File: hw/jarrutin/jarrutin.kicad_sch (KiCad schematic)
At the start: 24 parts, among them Q1 IR FET, Q2 IRFIZ34NPdF, U1 40106, U2 TC4422, U3 L7805, U4 Pico

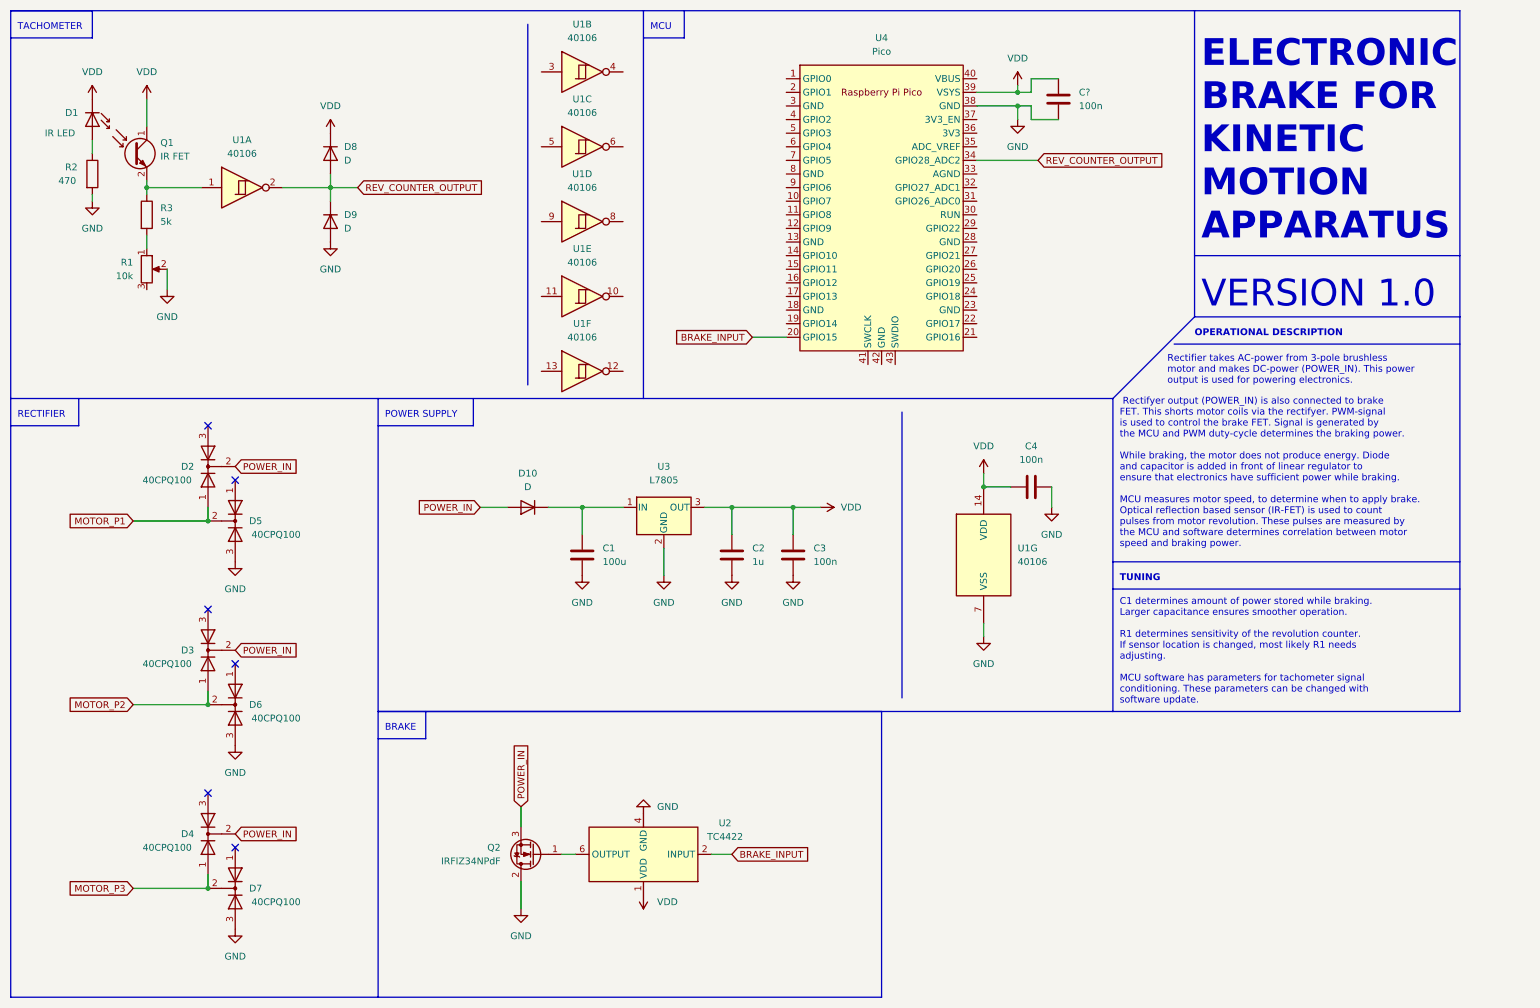
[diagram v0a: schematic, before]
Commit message: Adds BOM and updates HW design
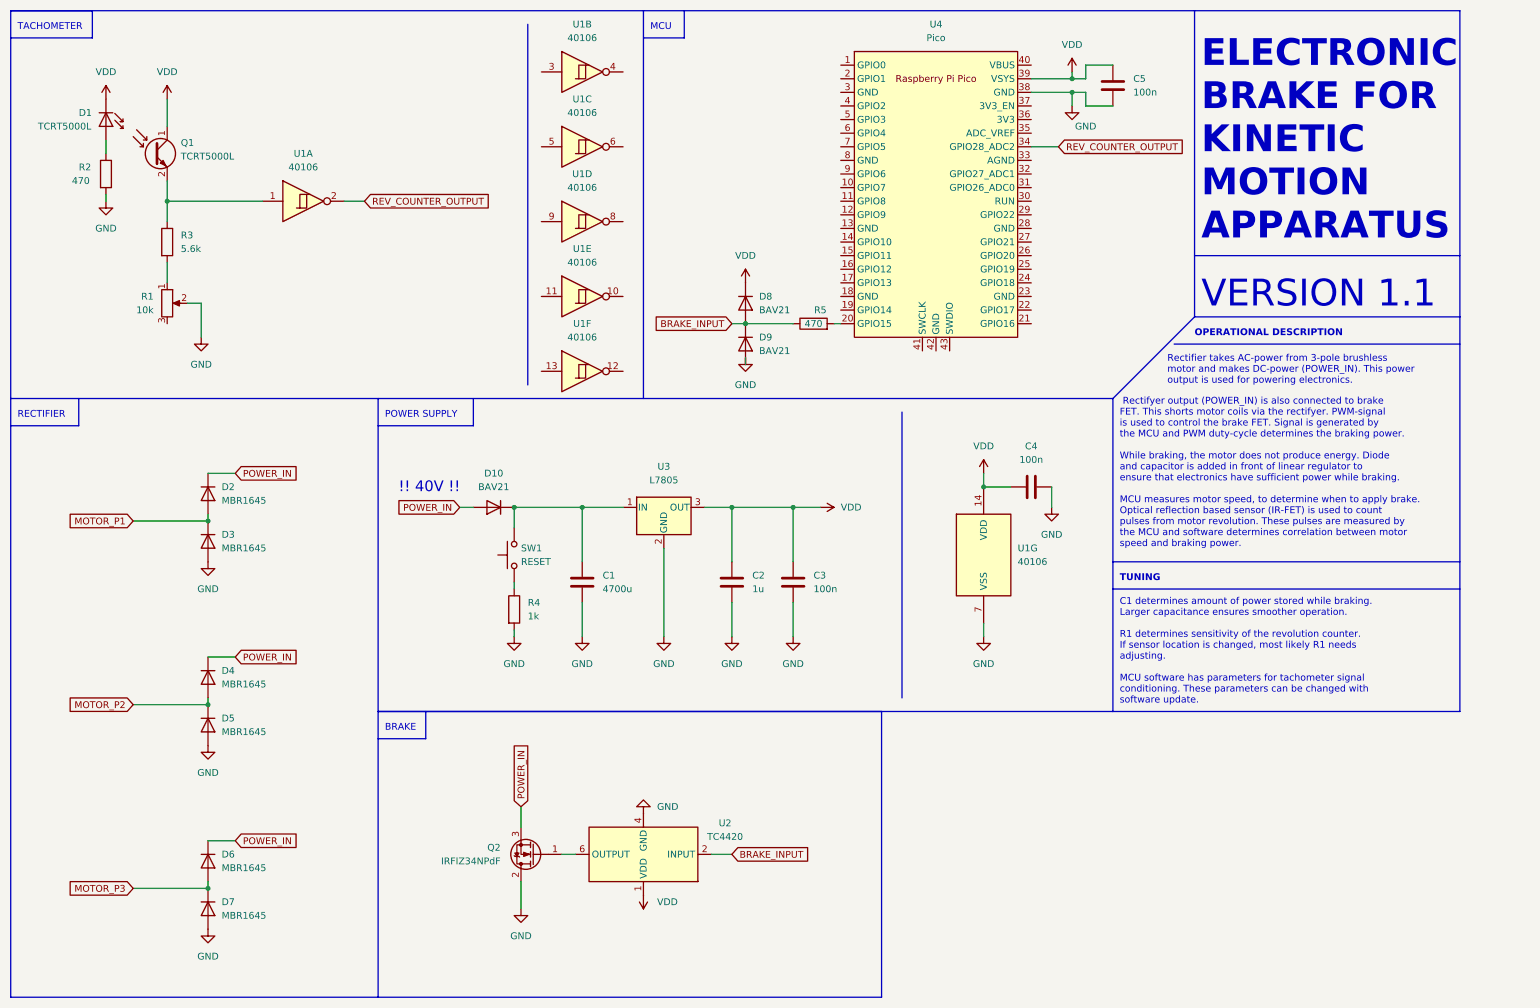
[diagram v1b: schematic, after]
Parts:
- removed D2, D3, D4, D5, D6, D7: 40CPQ100, Package_TO_SOT_THT:TO-247-3_Vertical, symbol Diode:BAV70W
- added D2, D3, D4, D5, D6, D7: MBR1645, symbol Device:D
- added R4: 1k, symbol Device:R
- added R5: 470, symbol Device:R
- added SW1: RESET, symbol Switch:SW_Push
- C1: value 100u -> 4700u
- D1: value IR LED -> TCRT5000L
- D10, D8, D9: value D -> BAV21
- Q1: value IR FET -> TCRT5000L
- R3: value 5k -> 5.6k
- U2: value TC4422 -> TC4420
- gave numbers to parts that had none: 1
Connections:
- net BRAKE_INPUT: now also D8.2 (A), D9.1 (K), R5.1; no longer U4.20 (GPIO15)
- net GND: now also D3.2 (A), D5.2 (A), D7.2 (A), R4.2
- net MOTOR_P1: now also D2.2 (A), D3.1 (K)
- net MOTOR_P2: now also D4.2 (A), D5.1 (K)
- net MOTOR_P3: now also D6.2 (A), D7.1 (K)
- net POWER_IN: now also D2.1 (K), D4.1 (K), D6.1 (K)
- net REV_COUNTER_OUTPUT: no longer D8.2 (A), D9.1 (K)
- net at C1.1, D10.1 (K), U3.1 (IN): now also SW1.2
- new net: R4.1, SW1.1
- new net: R5.2, U4.20 (GPIO15)
- no-connect marks 6 -> 0
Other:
- note added: "!! 40V !!"
- note added: "VERSION 1.1"
- note removed: "VERSION 1.0"
- moved on the sheet: C1, C2, C3, C5, D1, D10, Q1, R1, R2, R3, U1A, U4

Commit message: Updated schematic
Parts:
- added D11: INDICATOR, symbol LED:IR204A
- R4: value 1k -> 5.6k
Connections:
- net BRAKE_INPUT: now also U4.20 (GPIO15); no longer D8.2 (A), D9.1 (K), R5.1
- net GND: now also D11.1 (K)
- net REV_COUNTER_OUTPUT: now also D8.2 (A), D9.1 (K), R5.2; no longer U4.34 (GPIO28_ADC2)
- net at U4.4 (GPIO2): now also D11.2 (A)
- new net: R5.1, U4.34 (GPIO28_ADC2)
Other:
- note added: "C1 determines amount of power stored while braking. Larger capacitance ensures smoother operation. Too large capacitance will slow CPU boot-up time. R1 determines sensitivity of the revolution counter. If sensor location is changed, most likely R1 needs adjusting. 7.5kOhm (between pins 1 and 2) is good starting point. MCU software has parameters for tachometer signal conditioning. These parameter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"
- note added: "VERSION 1.2"
- note removed: "C1 determines amount of power stored while braking. Larger capacitance ensures smoother operation. R1 determines sensitivity of the revolution counter. If sensor location is changed, most likely R1 needs adjusting. MCU software has parameters for tachometer signal conditioning. These parameters can be changed with software update."
- note removed: "VERSION 1.1"
- moved on the sheet: C5, D8, D9, R5, U4

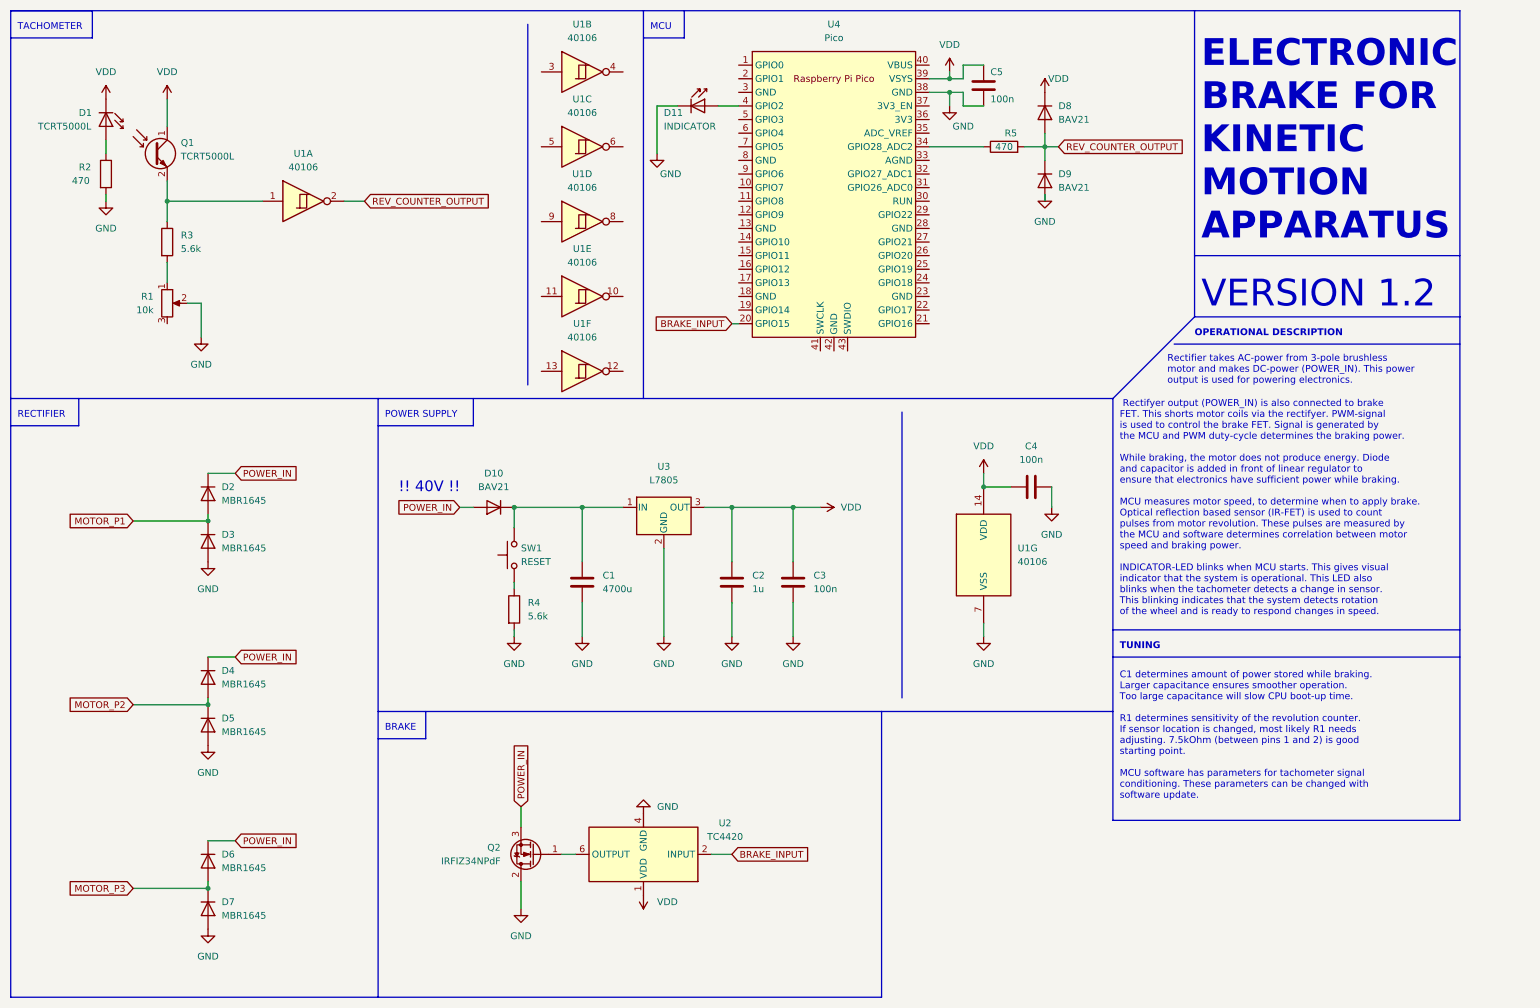
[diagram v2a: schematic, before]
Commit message: Update based on final implementation
Updated design, based on tests done 19.01.24. Functionality of hardware and software has been proven and the remaining issue is getting rid of dissipated power from diodes and FETs.
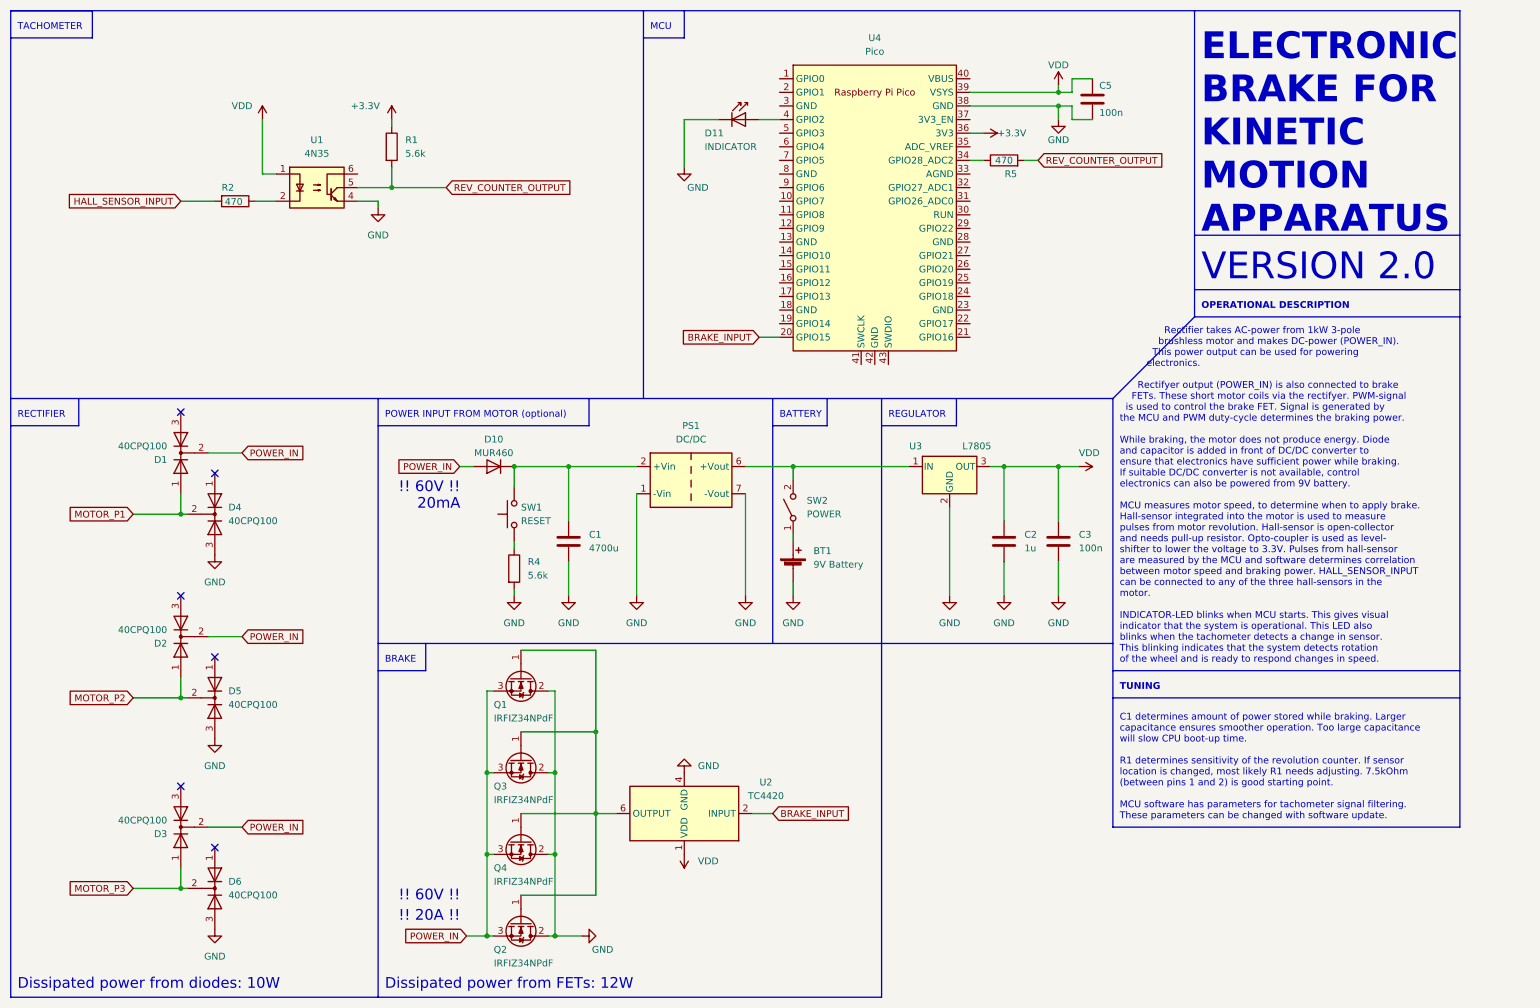
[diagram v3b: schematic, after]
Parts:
- removed C4: 100n, symbol Device:C
- removed D1: TCRT5000L, LED_THT:LED_D3.0mm_IRBlack, symbol LED:IR204A
- removed D2, D3, D4, D5, D6, D7: MBR1645, symbol Device:D
- removed D8, D9: BAV21, symbol Device:D
- removed Q1: TCRT5000L, LED_THT:LED_D5.0mm_Clear, symbol Sensor_Optical:BP103BF
- removed R1: 10k, symbol Device:R_Potentiometer
- removed R3: 5.6k, symbol Device:R
- removed U1: 40106, symbol 4xxx:40106
- added BT1: 9V Battery, symbol Device:Battery_Cell
- added D1, D2, D3, D4, D5, D6: 40CPQ100, symbol Device:D_Dual_CommonCathode_AAK
- added PS1: DC/DC, Converter_DCDC:Converter_DCDC_XP_POWER-ITXxxxxSA_THT, symbol Converter_DCDC:ITX0512SA
- added Q1, Q3, Q4: IRFIZ34NPdF, Package_TO_SOT_THT:TO-220-3_Vertical, symbol Transistor_FET:IRF540N
- added R1: 5.6k, symbol Device:R
- added SW2: POWER, symbol Switch:SW_SPST
- added U1: 4N35, Package_DIP:DIP-6_W7.62mm, symbol Isolator:4N35
- D10: value BAV21 -> MUR460
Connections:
- net GND: now also BT1.2 (-), D4.3 (A), D5.3 (A), D6.3 (A), PS1.1 (-Vin), PS1.7 (-Vout), Q1.2 (D), Q3.2 (D), Q4.2 (D), U1.4; no longer R2.2
- net MOTOR_P1: now also D1.1 (A), D4.2 (K)
- net MOTOR_P2: now also D2.1 (A), D5.2 (K)
- net MOTOR_P3: now also D3.1 (A), D6.2 (K)
- net POWER_IN: now also D1.2 (K), D2.2 (K), D3.2 (K), Q1.3 (S), Q3.3 (S), Q4.3 (S)
- net REV_COUNTER_OUTPUT: now also R1.2, U1.5
- net VDD: now also U1.1
- net at C1.1, D10.1 (K), SW1.2: now also PS1.2 (+Vin); no longer U3.1 (IN)
- net at R2.1: now also U1.2
- net at Q2.1 (G), U2.6 (OUTPUT), U2.7 (OUTPUT): now also Q1.1 (G), Q3.1 (G), Q4.1 (G)
- net +3.3V: now reaches U4.36 (3V3)
- net +3.3V: now also R1.1
- new net: BT1.1 (+), SW2.1 (A)
- new net: PS1.6 (+Vout), SW2.2 (B), U3.1 (IN)
- new net HALL_SENSOR_INPUT: R2.2
- no-connect marks 0 -> 6
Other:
- note added: "!! 20A !!"
- note added: "!! 60V !!"
- note added: "20mA"
- note added: "BATTERY"
- note added: "C1 determines amount of power stored while braking. Larger capacitance ensures smoother operation. Too large capacitance will slow CPU boot-up time. R1 determines sensitivity of the revolution counter. If sensor location is changed, most likely R1 needs adjusting. 7.5kOhm (between pins 1 and 2) is good starting point. MCU software has parameters for tachometer signal filtering. These parameters c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"
- note added: "Dissipated power from FETs: 12W"
- note added: "Dissipated power from diodes: 10W"
- note added: "POWER INPUT FROM MOTOR (optional)"
- note added: "REGULATOR"
- note added: "Rectifier takes AC-power from 1kW 3-pole brushless motor and makes DC-power (POWER_IN). This power output can be used for powering electronics. Rectifyer output (POWER_IN) is also connected to brake FETs. These short motor coils via the rectifyer. PWM-signal is used to control the brake FET. Signal is generated by the MCU and PWM duty-cycle determines the braking power. While braking, the motor d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"
- note added: "VERSION 2.0"
- note removed: "!! 40V !!"
- note removed: "C1 determines amount of power stored while braking. Larger capacitance ensures smoother operation. Too large capacitance will slow CPU boot-up time. R1 determines sensitivity of the revolution counter. If sensor location is changed, most likely R1 needs adjusting. 7.5kOhm (between pins 1 and 2) is good starting point. MCU software has parameters for tachometer signal conditioning. These parameter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"
- note removed: "POWER SUPPLY"
- note removed: "Rectifier takes AC-power from 3-pole brushless motor and makes DC-power (POWER_IN). This power output is used for powering electronics."
- note removed: "Rectifyer output (POWER_IN) is also connected to brake FET. This shorts motor coils via the rectifyer. PWM-signal is used to control the brake FET. Signal is generated by the MCU and PWM duty-cycle determines the braking power. While braking, the motor does not produce energy. Diode and capacitor is added in front of linear regulator to ensure that electronics have sufficient power while braking.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"
- note removed: "VERSION 1.2"
- moved on the sheet: C1, C2, C3, C5, D10, D11, Q2, R2, R4, R5, SW1, U2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
